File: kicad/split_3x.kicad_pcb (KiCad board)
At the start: 2 copper layers, 64 parts, among them SW1 SW_Push, SW2 SW_Push, SW3 Rotary_Encoder_Switch, SW4 Rotary_Encoder_Switch, U1 ProMicro, U2 TRRS

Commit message: replaced some things, added edgecuts
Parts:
- added REF**: MountingHole_2.2mm_M2_Pad_Via, MountingHole:MountingHole_2.2mm_M2_Pad_Via, F.Cu at (177.8, 66.7)
- added REF**: M2_Hole_TH_Outside, kbd:M2_Hole_TH_Outside, F.Cu at (190.5, 141.3)
- added REF**: M2_Hole_TH_Outside, kbd:M2_Hole_TH_Outside, F.Cu at (149.2, 113.5)
- added REF**: M2_Hole_TH_Outside, kbd:M2_Hole_TH_Outside, F.Cu at (134.9, 68.3)
- added REF**: M2_Hole_TH_Outside, kbd:M2_Hole_TH_Outside, F.Cu at (96.8, 85.7)
- added REF**: MountingHole_2.2mm_M2_Pad_Via, MountingHole:MountingHole_2.2mm_M2_Pad_Via, F.Cu at (200.8, 123.0)
- added REF**: MountingHole_2.2mm_M2_Pad_Via, MountingHole:MountingHole_2.2mm_M2_Pad_Via, F.Cu at (183.4, 112.7)
- JP5, JP6, JP7, JP8: moved to B.Cu
- moved JP2 118.8 mm to (173.2, 88.9), turned to 180 degrees
- moved D19 117.3 mm to (181.6, 137.5)
- moved JP7 115.1 mm to (173.0, 92.1), turned to 180 degrees
- moved JP5 114.1 mm to (173.0, 85.7), turned to 180 degrees
- moved D16 109.3 mm to (171.6, 71.5)
- moved JP3 108.6 mm to (173.2, 92.1), turned to 180 degrees
- moved D15 108.4 mm to (157.6, 120.5)
- moved JP1 105.7 mm to (173.2, 85.7), turned to 180 degrees
- moved JP8 103.7 mm to (173.0, 95.2), turned to 180 degrees
- moved JP4 102.1 mm to (173.2, 95.2), turned to 180 degrees
- moved JP6 99.9 mm to (173.0, 88.9), turned to 180 degrees
- moved D12 98.9 mm to (154.0, 64.3)
- moved D18 98.0 mm to (171.6, 108.5)
- moved D17 96.4 mm to (166.6, 90.5)
- moved D13 87.0 mm to (152.6, 87.5)
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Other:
- board outline added: 127.3 x 121.2 mm

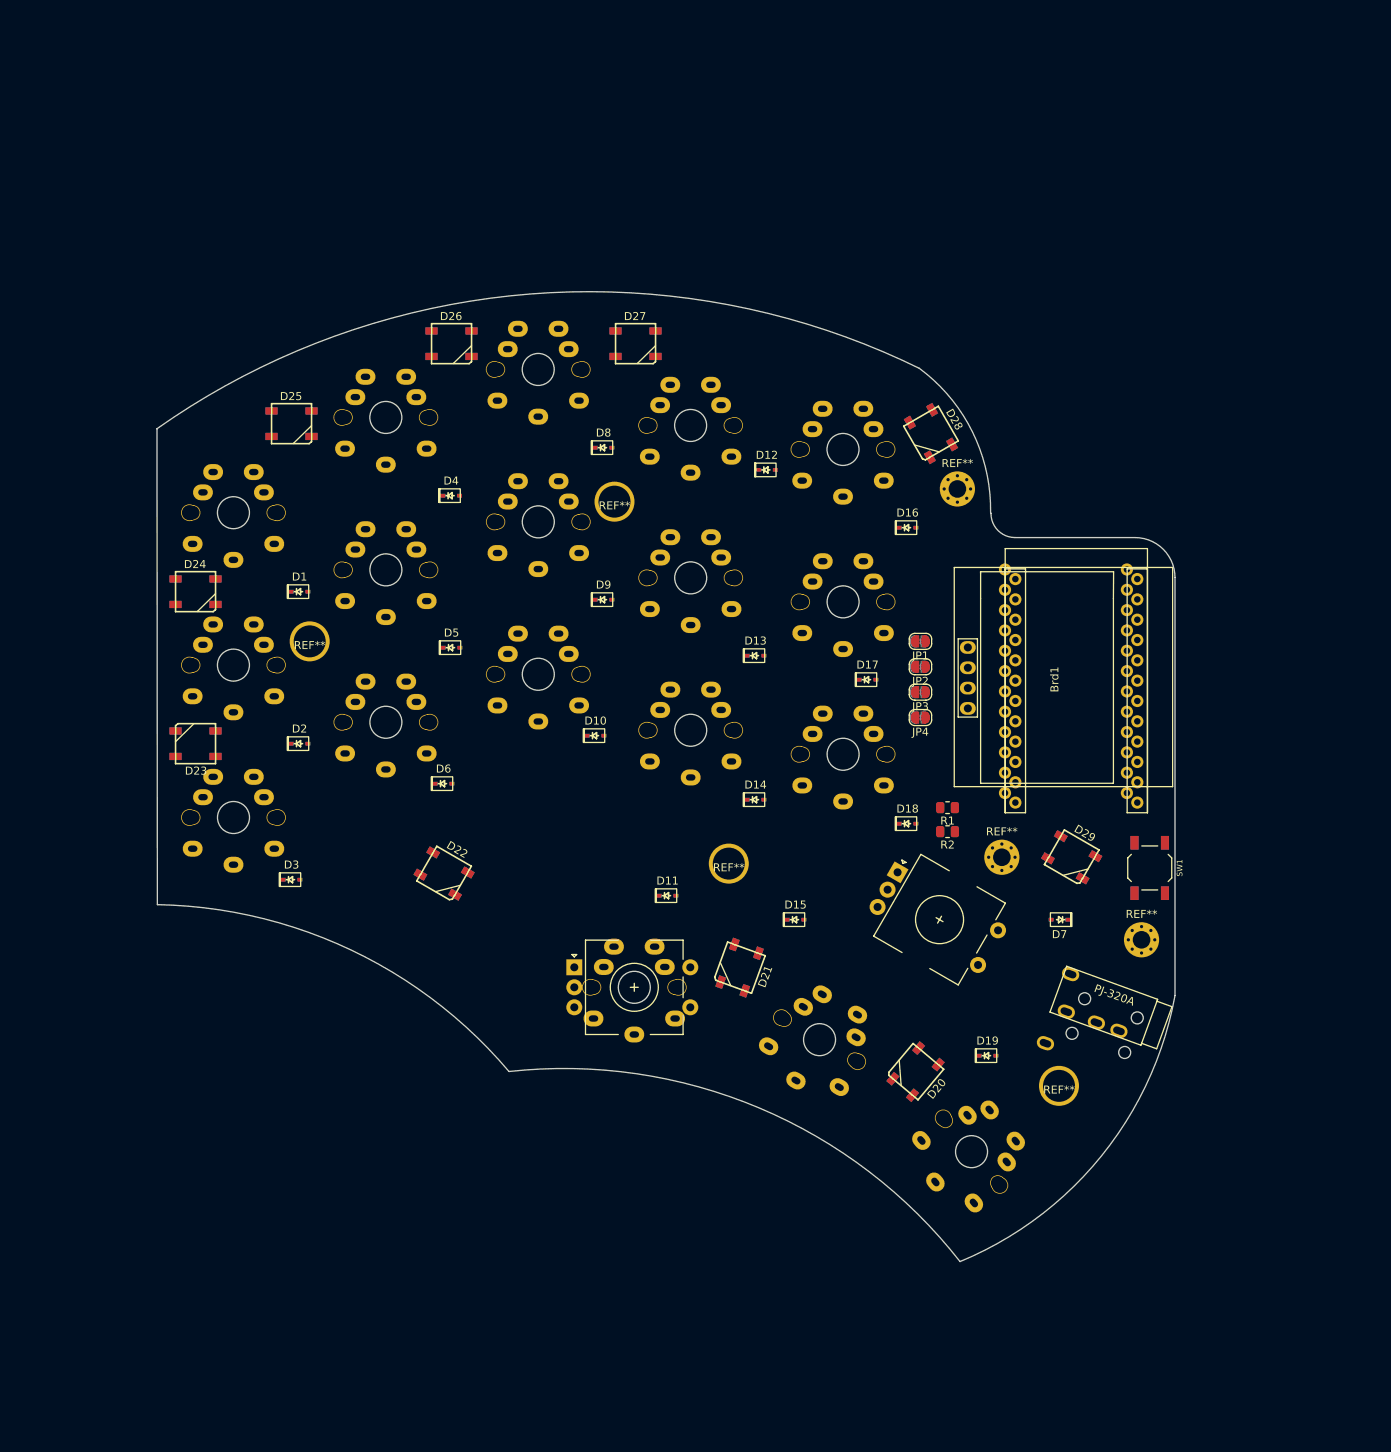
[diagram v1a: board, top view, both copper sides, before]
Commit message: added some routing
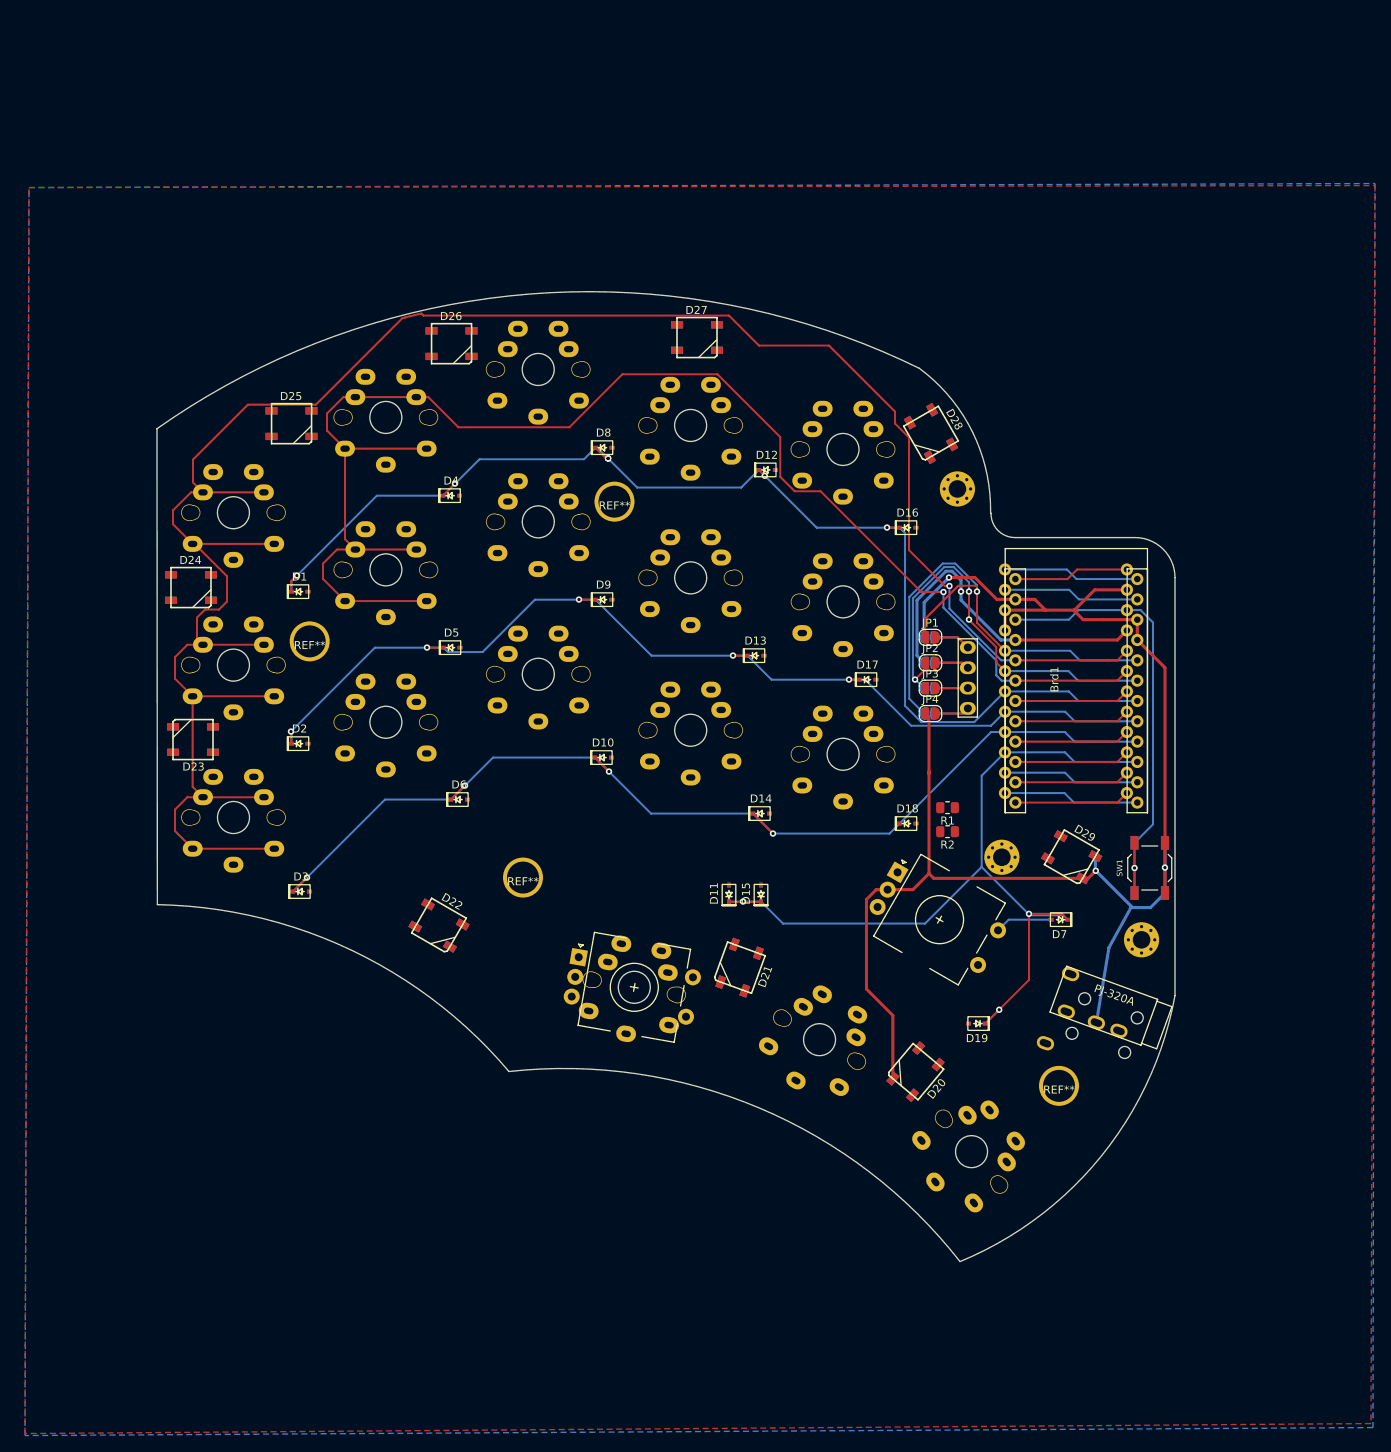
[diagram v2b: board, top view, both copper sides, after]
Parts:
-  : renamed from REF** (x3)
- moved REF** 25.8 mm to (123.5, 115.2)
- moved D27 7.72 mm to (145.2, 47.8)
- moved D11 7.69 mm to (149.2, 117.2), turned to 90 degrees
- moved D22 6.53 mm to (113.0, 121.2)
- moved D15 5.41 mm to (153.2, 117.2), turned to 90 degrees
- moved D19 4.22 mm to (180.2, 133.5), turned to 180 degrees
- moved D10 2.89 mm to (133.5, 100.2)
- moved D6 2.77 mm to (115.5, 105.5)
- moved D3 1.90 mm to (95.8, 117.0)
- moved D14 1.87 mm to (153.2, 107.2)
- moved JP1 1.35 mm to (174.4, 85.2), turned to 0 degrees
- moved JP2 1.35 mm to (174.4, 88.4), turned to 0 degrees
- moved JP3 1.35 mm to (174.4, 91.6), turned to 0 degrees
- moved JP4 1.35 mm to (174.4, 94.8), turned to 0 degrees
- moved JP5 1.35 mm to (174.3, 85.2), turned to 0 degrees
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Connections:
- U1 pad 15: col4 -> Net-(U1-Pad15)
- U1 pad 16: col3 -> col4
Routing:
- net col0: track 0.00 -> 271.8 mm, vias 0 -> 1
- net ground: track 0.00 -> 195.2 mm, vias 0 -> 3
- net col1: track 0.00 -> 183.7 mm, vias 0 -> 1
- net row0: track 0.00 -> 154.0 mm, vias 0 -> 6
- net row2: track 0.00 -> 133.3 mm, vias 0 -> 4
- net row1: track 0.00 -> 130.9 mm, vias 0 -> 5
- net row3: track 0.00 -> 109.3 mm, vias 0 -> 3
- net sda: track 0.00 -> 64.5 mm, vias 0 -> 1
- net reset: track 0.00 -> 59.4 mm, vias 0 -> 1
- net scl: track 0.00 -> 53.8 mm, vias 0 -> 3
- net power: track 0.00 -> 41.4 mm, vias 0 -> 1
- net enc1db: track 0.00 -> 17.0 mm
- net enc1da: track 0.00 -> 17.0 mm
- net connection: track 0.00 -> 17.0 mm
- net leds: track 0.00 -> 17.0 mm
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- added copper zone on B.Cu, net (none)
- added copper zone on F.Cu, net ground
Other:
- net class Power added: clearance 0.2, trace_width 0.381, via_dia 0.8, via_drill 0.4
- net class TRRSData added: clearance 0.2, trace_width 0.381, via_dia 0.8, via_drill 0.4

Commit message: finished routing
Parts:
- moved   0.97 mm to (200.8, 124.0)
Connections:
- D20 pad 4: leds -> Net-(D20-Pad4)
- D29 pad 2: Net-(D29-Pad2) -> Net-(D20-Pad4)
- D29 pad 4: Net-(D28-Pad2) -> leds
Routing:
- net power: track 41.4 -> 491.8 mm, vias 1 -> 19
- net col2: track 14.4 -> 256.3 mm, vias 0 -> 3
- net col4: track 14.4 -> 225.7 mm, vias 0 -> 4
- net col3: track 14.4 -> 225.4 mm, vias 0 -> 1
- net col1: track 183.7 -> 309.5 mm, vias 1 -> 3
- net enc1db: track 17.0 -> 133.2 mm, vias 0 -> 1
- net enc1da: track 17.0 -> 123.2 mm
- net leds: track 17.0 -> 77.0 mm, vias 0 -> 2
- net connection: track 17.0 -> 76.4 mm, vias 0 -> 3
- net Net-(D22-Pad2): track 0.00 -> 58.5 mm, vias 0 -> 2
- net Net-(D20-Pad2): track 0.00 -> 55.3 mm, vias 0 -> 3
- net Net-(D20-Pad4): track 0.00 -> 52.8 mm, vias 0 -> 7
- net Net-(D26-Pad2): track 0.00 -> 51.7 mm, vias 0 -> 3
- net Net-(D27-Pad2): track 0.00 -> 47.4 mm, vias 0 -> 2
- net enc0da: track 14.4 -> 59.4 mm, vias 0 -> 1
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- added copper zone on B.Cu, net ground
- removed copper zone on B.Cu, net (none)

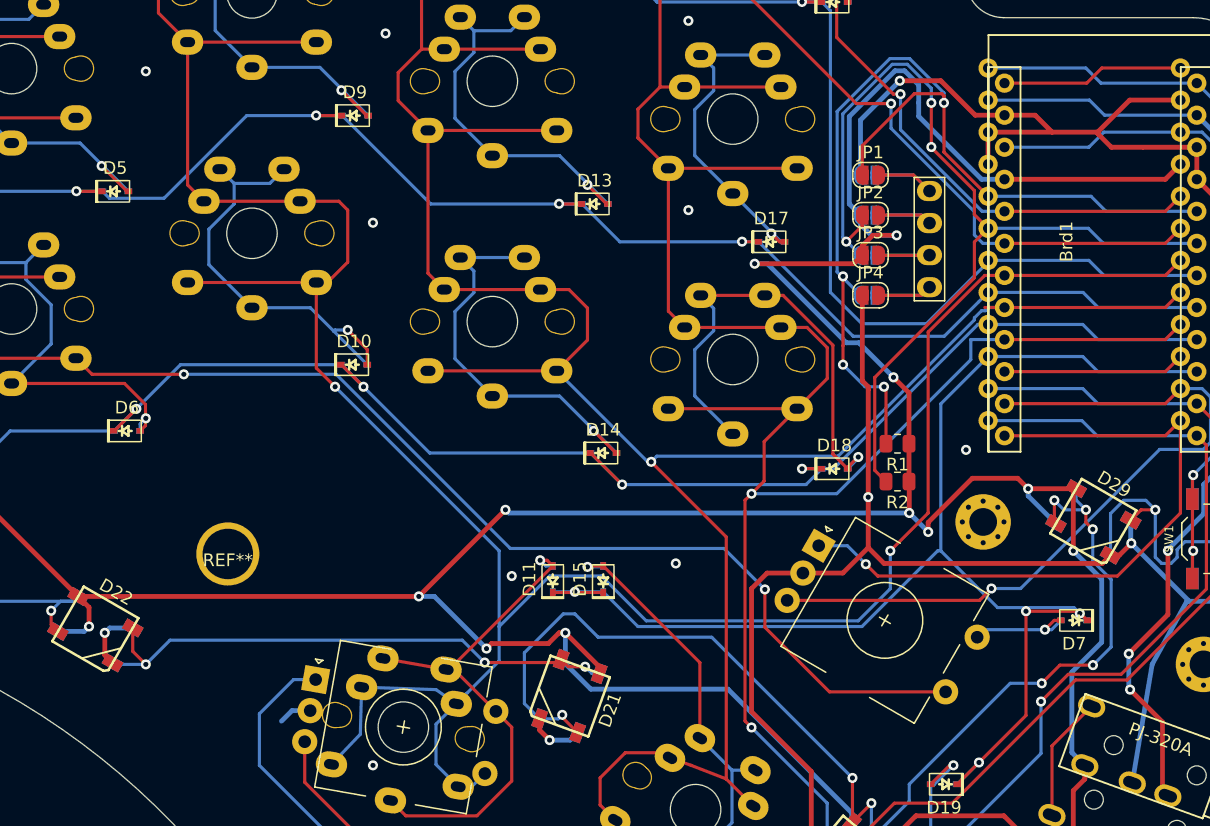
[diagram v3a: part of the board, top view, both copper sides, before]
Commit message: added art and text
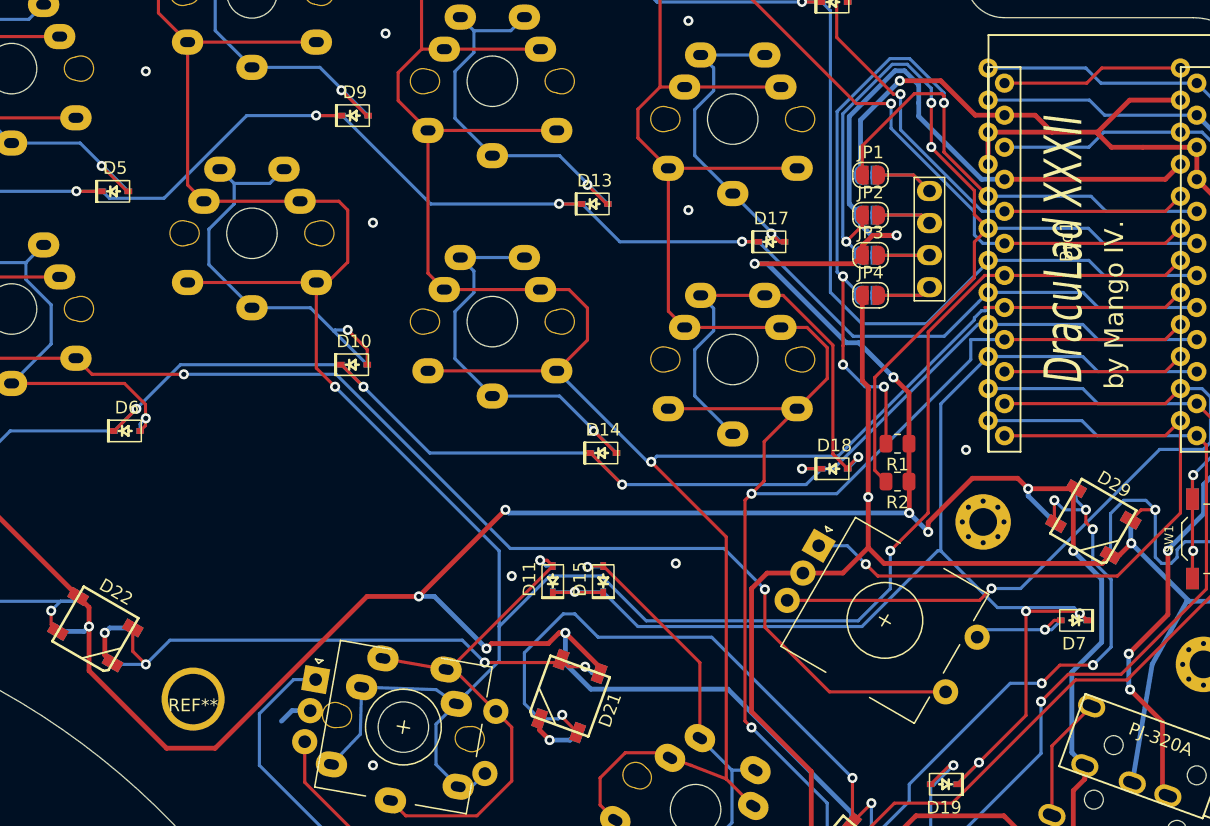
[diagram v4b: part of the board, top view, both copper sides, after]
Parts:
- added G***: LOGO, graphics:aset, B.Cu at (125.2, 113.2)
- added G***: LOGO, graphics:aset, F.Cu at (123.8, 113.0)
- moved REF** 11.8 mm to (120.8, 126.8)
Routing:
- net power: track 491.8 -> 502.0 mm
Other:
- board text added: "DracuLad XXXII"
- board text added: "by Mango IV."
